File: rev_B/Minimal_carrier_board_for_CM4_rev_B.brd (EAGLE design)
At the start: 71.1 x 63.5 mm, 22 parts, among them IC1 MC74VHC1G14DFT1G, J1 P1-100, J2 P101-200, J6 629104190121

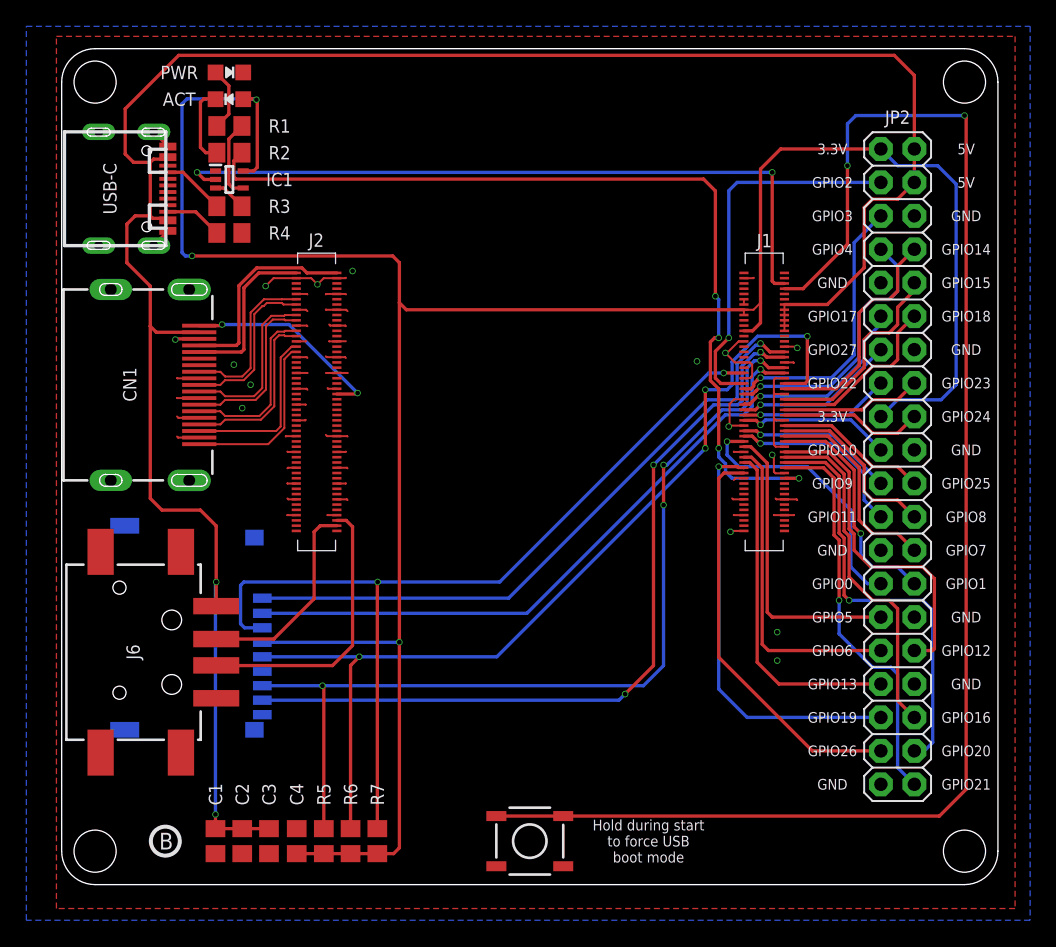
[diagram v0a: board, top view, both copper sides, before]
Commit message: Added connector for camera and DSI display
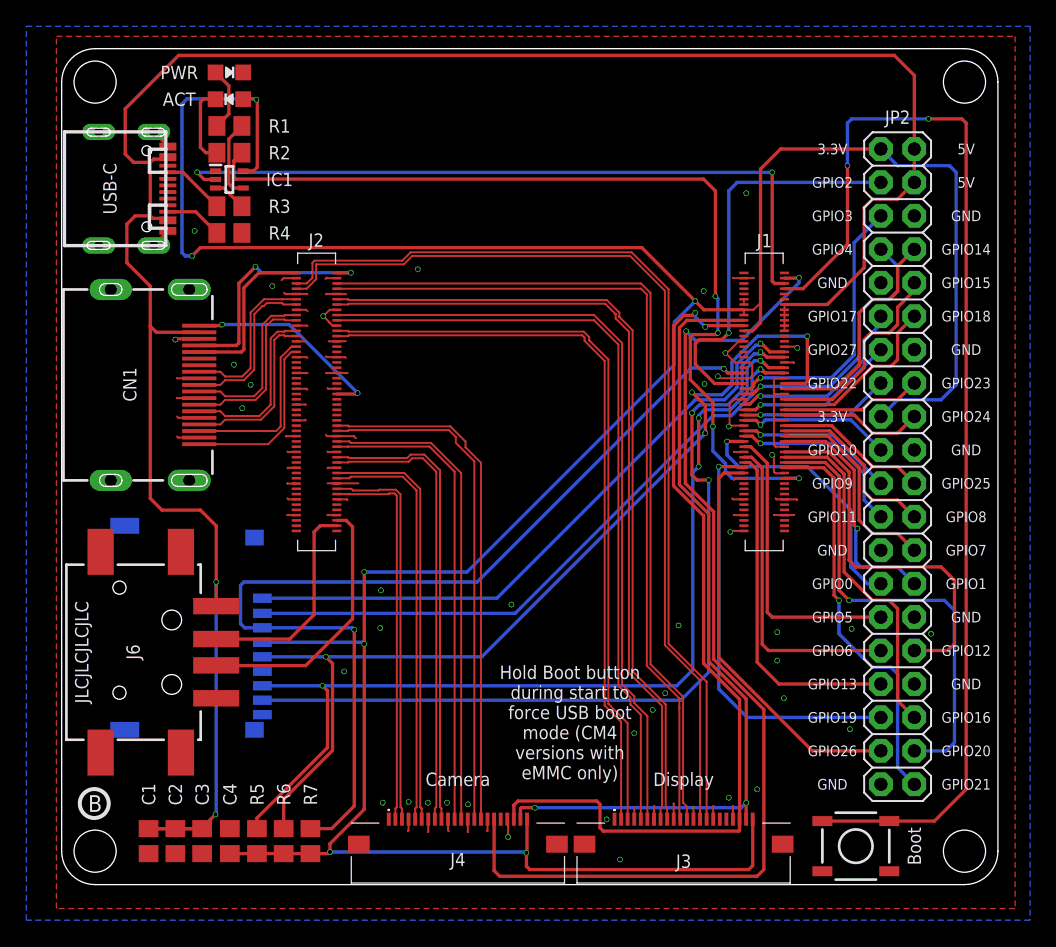
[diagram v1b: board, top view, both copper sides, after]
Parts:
- removed U$65: TACTILE_SWITCHE_5X5_MICRO_, dronecz:TACTILE_SWITCH_5X5_MICRO
- added BOOT: TACTILE_SWITCHE_5X5_MICRO_, dronecz:TACTILE_SWITCH_5X5_MICRO
- added J3, J4: 54548-2271, dronecz:545482271
- moved C4 5.08 mm to (12.8, 3.30)
- moved C2 5.08 mm to (8.64, 3.30)
- moved C3 5.08 mm to (10.7, 3.30)
- moved C1 5.08 mm to (6.60, 3.30)
- moved R5 5.08 mm to (14.8, 3.30)
- moved R6 5.08 mm to (16.9, 3.30)
- moved R7 5.08 mm to (18.9, 3.30)
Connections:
- new net N$24: J3.17
- new net N$25: J3.18
- net 3.3V: now also J3.22, J4.22
- net CAM1_C_N: now also J4.8
- net CAM1_C_P: now also J4.9
- net CAM1_D0_N: now also J4.2
- net CAM1_D0_P: now also J4.3
- net CAM1_D1_N: now also J4.5
- net CAM1_D1_P: now also J4.6
- net CAM1_D2_N: now also J4.11
- net CAM1_D2_P: now also J4.12
- net CAM1_D3_N: now also J4.14
- net CAM1_D3_P: now also J4.15
- net CAM_GPIO: now also J4.17
- net DSI1_C_N: now also J3.8
- net DSI1_C_P: now also J3.9
- net DSI1_D0_N: now also J3.2
- net DSI1_D0_P: now also J3.3
- net DSI1_D1_N: now also J3.5
- net DSI1_D1_P: now also J3.6
- net DSI1_D2_N: now also J3.11
- net DSI1_D2_P: now also J3.12
- net DSI1_D3_N: now also J3.14
- net DSI1_D3_P: now also J3.15
- net GND: now also BOOT.3, BOOT.4, J3.1, J3.10, J3.13, J3.16, J3.19, J3.4, J3.7, J4.1, J4.10, J4.13, J4.16, J4.19, J4.4, J4.7; no longer U$65.3, U$65.4
- net N_RPIBOOT: now also BOOT.1, BOOT.2; no longer U$65.1, U$65.2
- net SCL0: now also J3.20, J4.20
- net SDA0: now also J3.21, J4.21
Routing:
- net CAM_GPIO: track 0.00 -> 80.4 mm, vias 0 -> 2
- net DSI1_D3_P: track 0.00 -> 72.5 mm
- net DSI1_D3_N: track 0.00 -> 72.0 mm
- net SCL0: track 0.00 -> 67.2 mm, vias 0 -> 2
- net DSI1_D2_P: track 0.00 -> 65.2 mm
- net DSI1_D2_N: track 0.00 -> 64.6 mm
- net SDA0: track 0.00 -> 62.7 mm, vias 0 -> 2
- net DSI1_C_P: track 0.00 -> 61.9 mm
- net DSI1_C_N: track 0.00 -> 61.4 mm
- net DSI1_D1_P: track 0.00 -> 59.5 mm
- net DSI1_D1_N: track 0.00 -> 58.9 mm
- net DSI1_D0_P: track 0.00 -> 57.2 mm
- net DSI1_D0_N: track 0.00 -> 56.6 mm
- net 3.3V: track 184.2 -> 236.5 mm, vias 3 -> 7
- net CAM1_D3_P: track 0.00 -> 39.4 mm
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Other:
- board text added: "Boot"
- board text added: "Camera"
- board text added: "Display"
- board text added: "Hold Boot button during start to force USB boot mode (CM4 versions with eMMC only)"
- board text added: "JLCJLCJLCJLC"
- board text removed: "Hold during start to force USB boot mode"

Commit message: Update
- moved USB-C, HDMI and USB-A connector to ensure that cables will not colide
- changed USB-C and HDMI connector to my library so I can display width od the connectors
- updated README accordingly
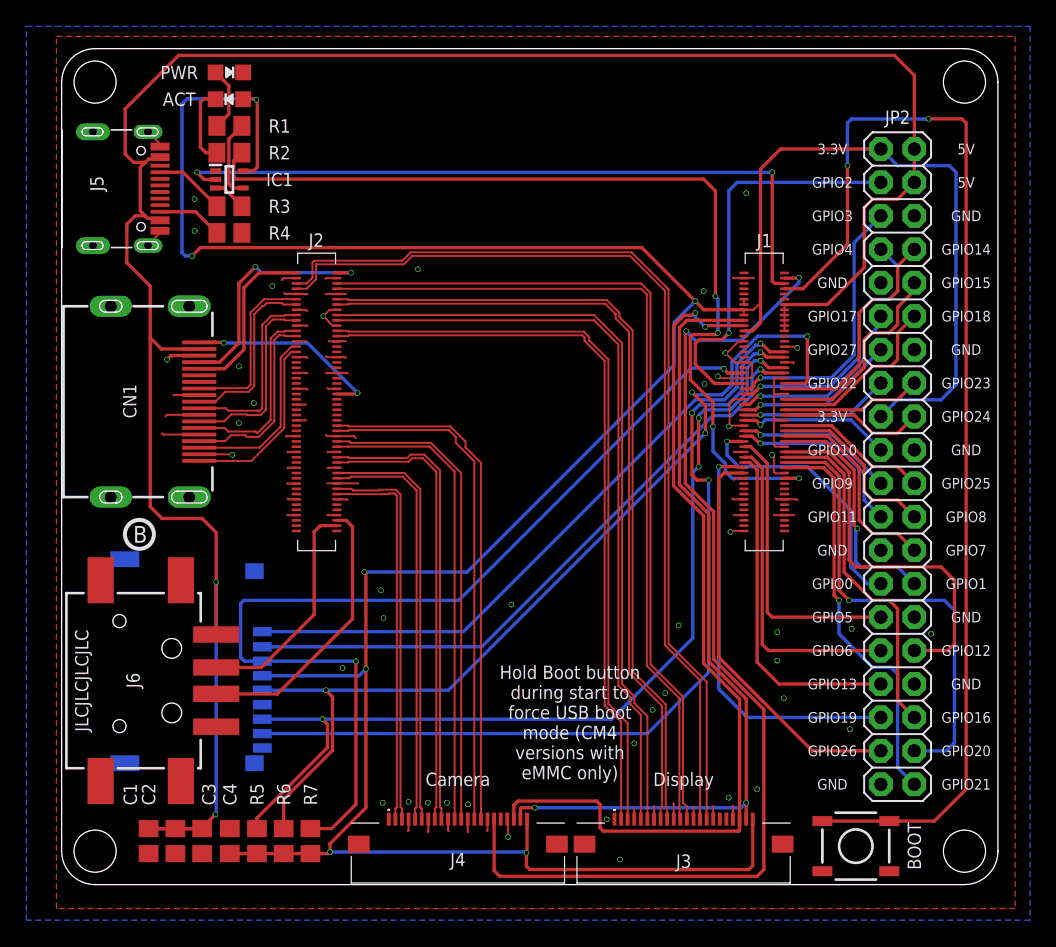
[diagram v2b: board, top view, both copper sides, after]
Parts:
- removed USB-C: TYPE-C-31-M-12, Custom-Parts:USB-TYPE-C_16PIN-MALE-TYPE-C-31-M-12
- added J5: HRO_31_M_12_USB_C, dronecz:HRO_31_M_12_USB_C
- CN1: device microbuilder:HDMI_MOLEX_47151-0001 -> dronecz:HDMI_MOLEX_47151-0001
- J6: device Wurth_Connectors_WR-USB:629104190121 -> dronecz:629104190121
- moved SD_CARD 2.54 mm to (7.39, 17.0)
- moved J6 2.16 mm to (5.46, 15.5)
- moved CN1 1.27 mm to (10.4, 36.7)
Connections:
- removed net N$8: R3.2, USB-C.A5
- new net N$5: J5.A5, R3.2
- net 5.0V: now also J5.A4, J5.A9, J5.B4, J5.B9; no longer USB-C.A4, USB-C.A9, USB-C.B4, USB-C.B9
- net GND: now also J5.A1, J5.A12, J5.B1, J5.B12, J5.S1, J5.S2, J5.S3, J5.S4; no longer USB-C.0, USB-C.0-1, USB-C.0-2, USB-C.0-3, USB-C.A1, USB-C.A12, USB-C.B1, USB-C.B12
- net N$3: now also J5.B5; no longer USB-C.B5
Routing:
- net N$5: track 0.00 -> 5.38 mm
- net GND: track 92.1 -> 97.2 mm, vias 41 -> 43
- net N$8: track 4.79 -> 0.00 mm
- net SD_DAT0: track 75.5 -> 72.6 mm
- net 5.0V: track 168.6 -> 170.2 mm
- net SD_CLK: track 76.0 -> 74.5 mm
- net HDMI0_D0_P: track 12.9 -> 14.4 mm
- net HDMI0_D0_N: track 12.9 -> 14.2 mm
- net HDMI0_D1_P: track 13.2 -> 14.5 mm
- net HDMI0_CK_P: track 12.5 -> 13.7 mm
- net HDMI0_D1_N: track 13.2 -> 14.4 mm
- net SD_DAT1: track 65.8 -> 66.8 mm
- net SD_DAT3: track 48.3 -> 49.3 mm
- net SD_DAT2: track 49.0 -> 50.0 mm
- net HDMI0_CK_N: track 12.4 -> 13.4 mm
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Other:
- board text added: "BOOT"
- board text removed: "Boot"
